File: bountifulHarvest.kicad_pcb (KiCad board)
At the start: 2 copper layers, 17 parts, among them U1 ATmega2560-16AU, U10 TMC2130-LA, U2 STM32F303CBTx, U3 TPS5431DDA, U4 AMS1117-3.3, U6 TMC2130-LA, U7 TMC2130-LA, U8 TMC2130-LA, U9 TMC2130-LA

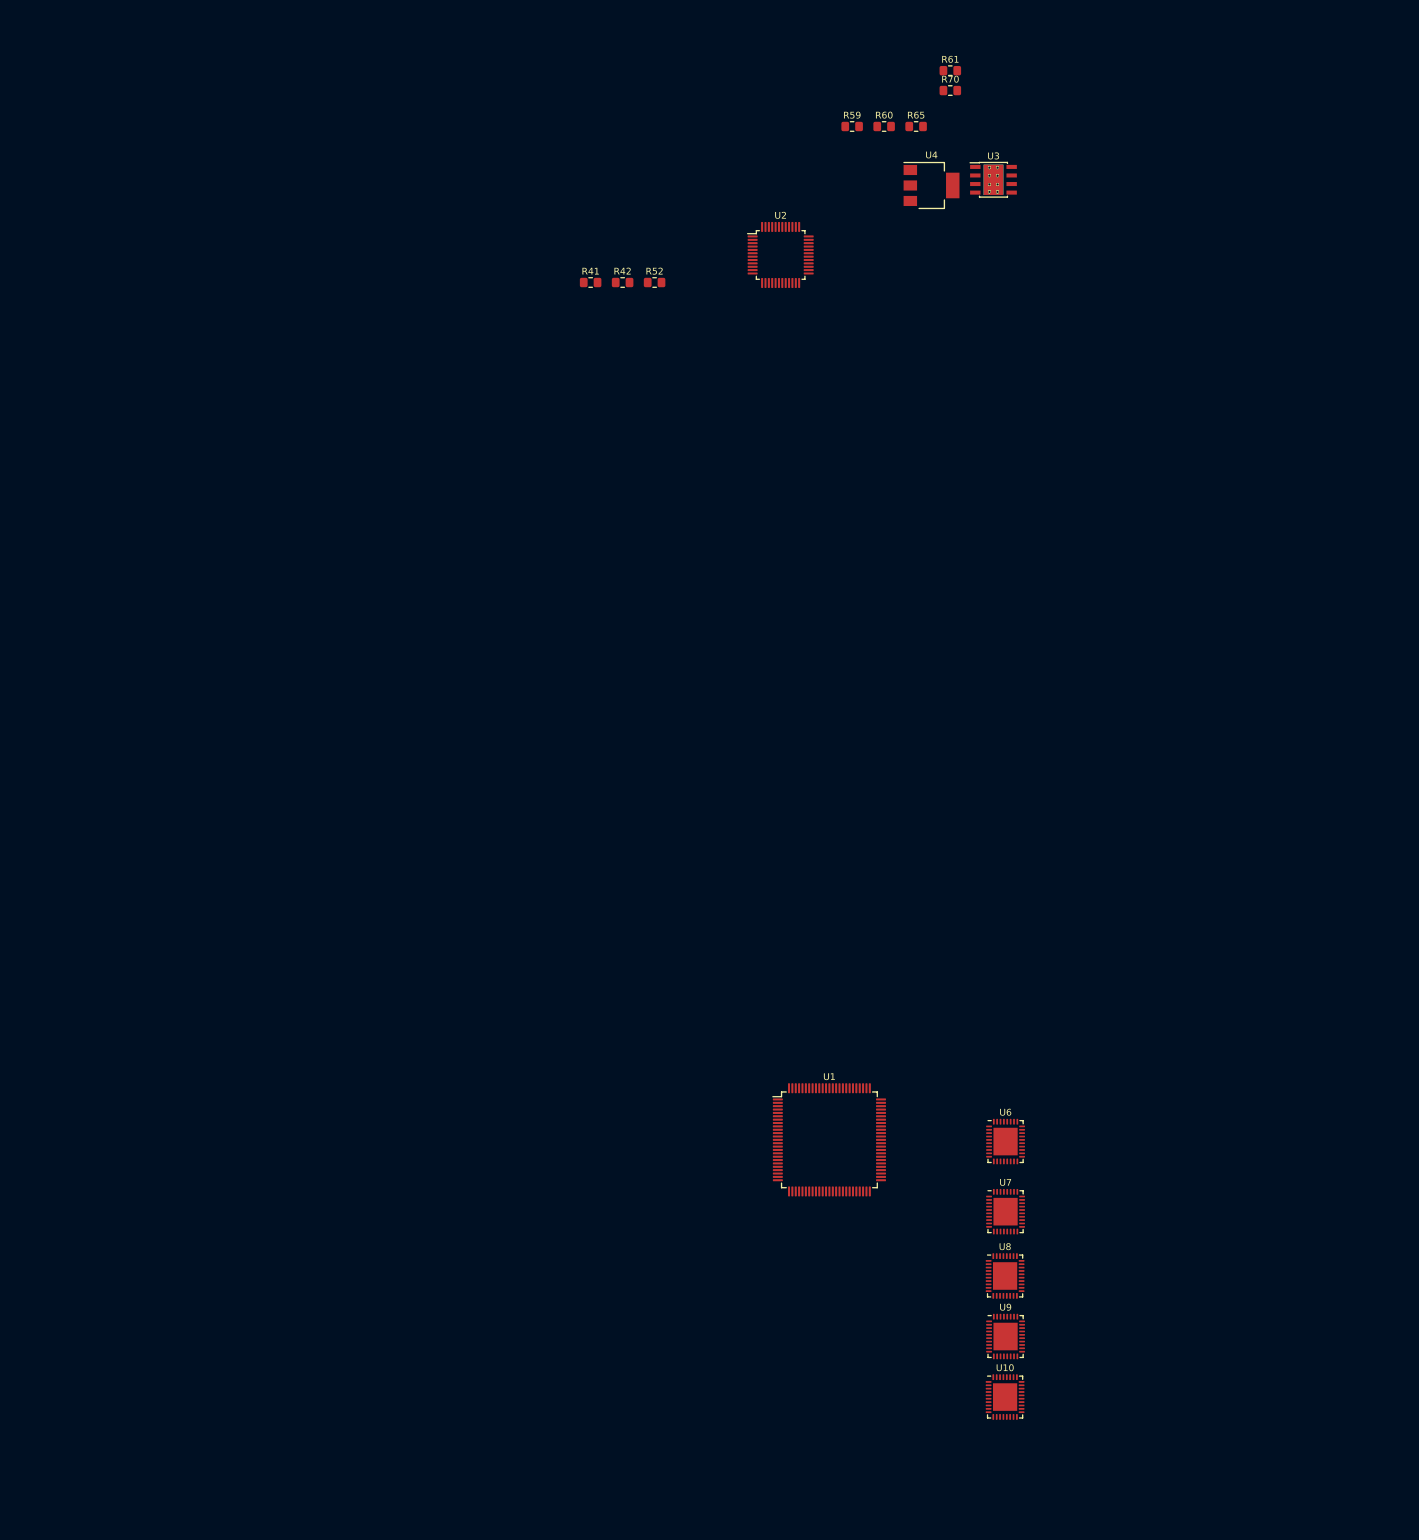
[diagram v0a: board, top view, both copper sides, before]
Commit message: Updated bus connections between drivers at ATMega
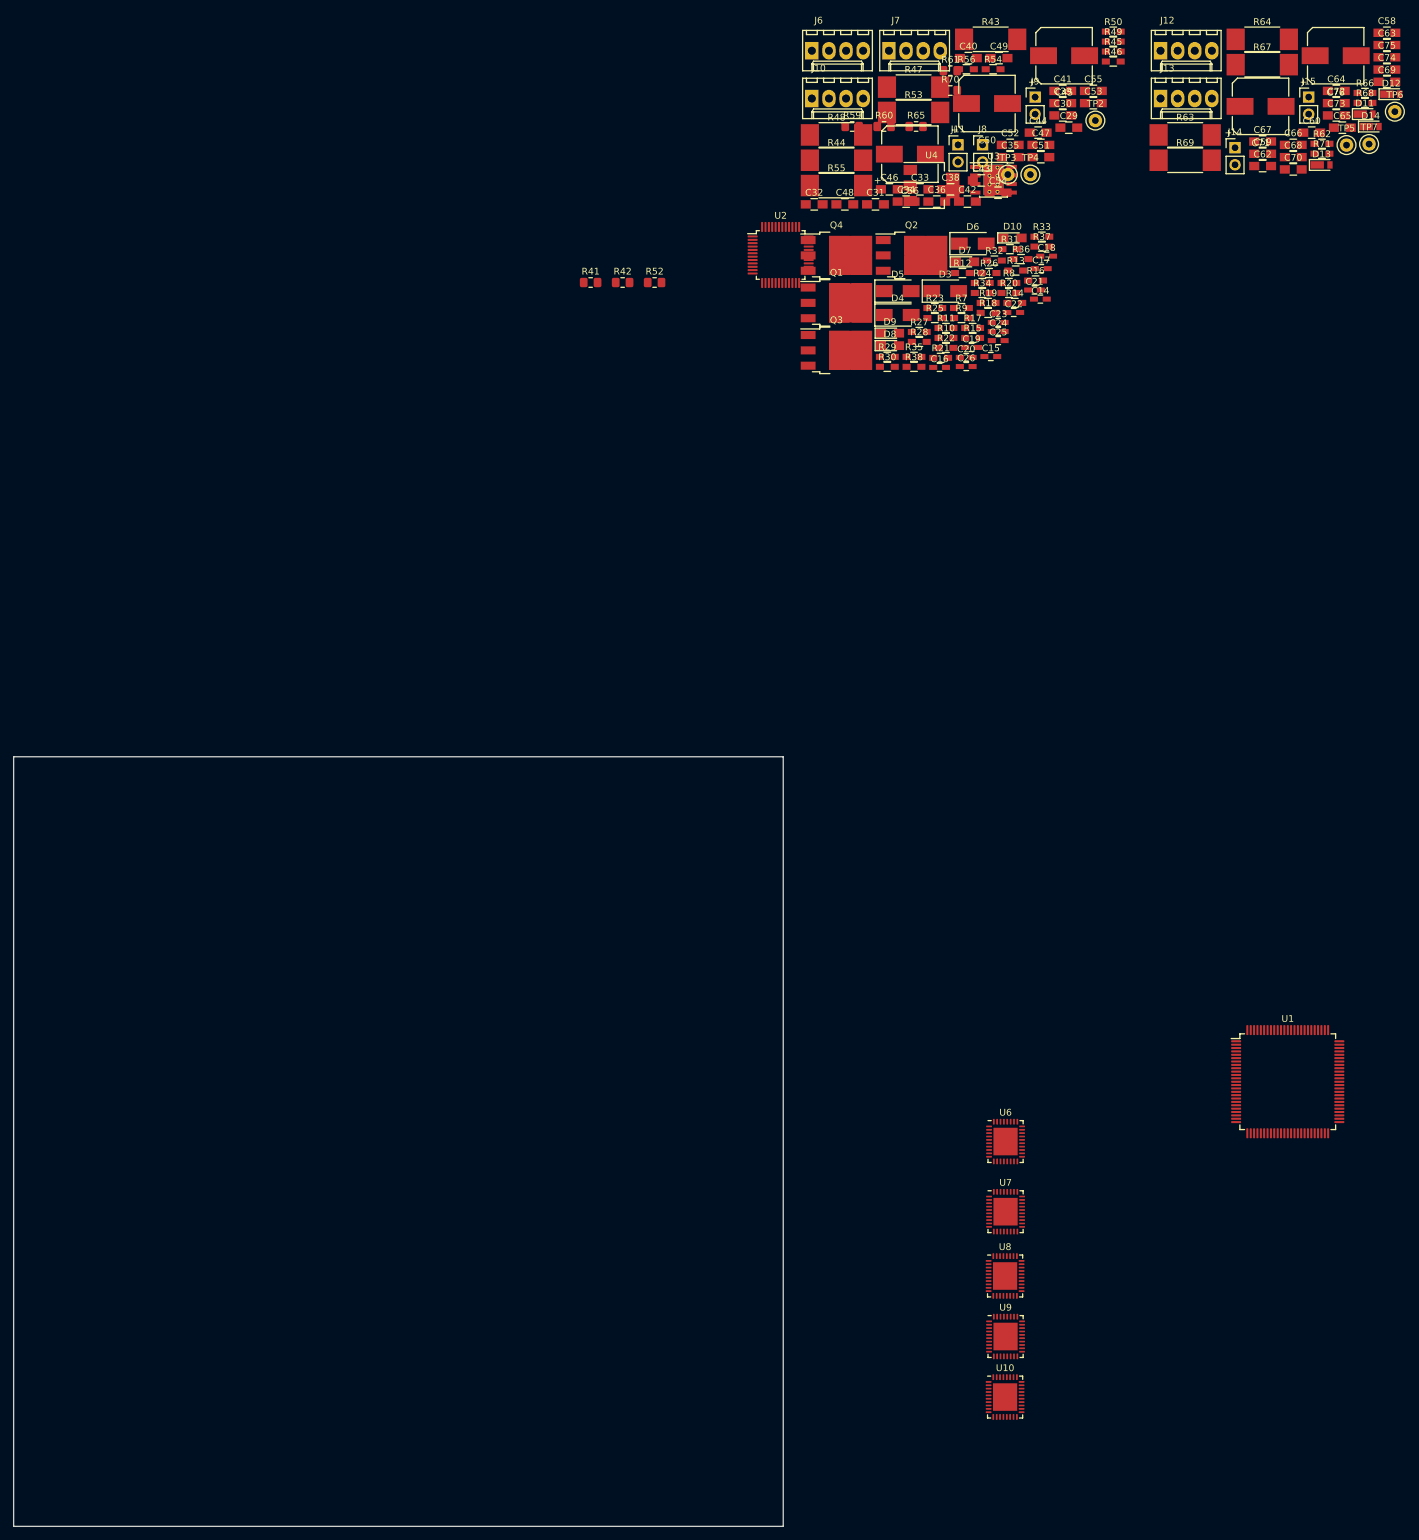
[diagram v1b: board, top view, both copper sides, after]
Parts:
- added C14: 1nF, Capacitors_SMD:C_0603_HandSoldering, F.Cu at (177.9, -42.6)
- added C15: 1nF, Capacitors_SMD:C_0603_HandSoldering, F.Cu at (170.5, -34.0)
- added C16: 1nF, Capacitors_SMD:C_0603_HandSoldering, F.Cu at (162.9, -32.4)
- added C17: 1nF, Capacitors_SMD:C_0603_HandSoldering, F.Cu at (178.0, -47.1)
- added C18: 100pF, Capacitors_SMD:C_0603_HandSoldering, F.Cu at (178.8, -48.9)
- added C19: 100pF, Capacitors_SMD:C_0603_HandSoldering, F.Cu at (167.7, -35.4)
- added C20: 100pF, Capacitors_SMD:C_0603_HandSoldering, F.Cu at (166.9, -33.9)
- added C21: 100pF, Capacitors_SMD:C_0603_HandSoldering, F.Cu at (177.0, -43.9)
- added C22: 100pF, Capacitors_SMD:C_0603_HandSoldering, F.Cu at (173.9, -40.6)
- added C23: 100pF, Capacitors_SMD:C_0603_HandSoldering, F.Cu at (171.6, -39.1)
- added C24: 100pF, Capacitors_SMD:C_0603_HandSoldering, F.Cu at (171.6, -37.8)
- added C25: 100pF, Capacitors_SMD:C_0603_HandSoldering, F.Cu at (171.6, -36.4)
- added C26: 1nF, Capacitors_SMD:C_0603_HandSoldering, F.Cu at (166.9, -32.6)
- added C29: 4.7uF, Capacitors_SMD:C_0805_HandSoldering, F.Cu at (182.1, -68.0)
- added C30: 4.7uF, Capacitors_SMD:C_0805_HandSoldering, F.Cu at (181.2, -69.9)
- added C31: 100nF, Capacitors_SMD:C_0805_HandSoldering, F.Cu at (153.4, -56.6)
- added C32: 100nF, Capacitors_SMD:C_0805_HandSoldering, F.Cu at (144.3, -56.6)
- added C33: 100nF, Capacitors_SMD:C_0805_HandSoldering, F.Cu at (160.0, -58.9)
- added C34: 100nF, Capacitors_SMD:C_0805_HandSoldering, F.Cu at (157.9, -57.1)
- added C35: 22nF, Capacitors_SMD:C_0805_HandSoldering, F.Cu at (173.4, -63.7)
- added C36: 22nF, Capacitors_SMD:C_0805_HandSoldering, F.Cu at (162.5, -57.1)
- added C38: 4.7uF, Capacitors_SMD:C_0805_HandSoldering, F.Cu at (164.6, -58.9)
- added C39: 100nF, Capacitors_SMD:C_0805_HandSoldering, F.Cu at (181.2, -71.7)
- added C40: 100nF, Capacitors_SMD:C_0805_HandSoldering, F.Cu at (167.2, -78.4)
- added C41: 100nF, Capacitors_SMD:C_0805_HandSoldering, F.Cu at (181.2, -73.5)
- added C42: 100nF, Capacitors_SMD:C_0805_HandSoldering, F.Cu at (167.0, -57.1)
- added C43: 100nF, Capacitors_SMD:C_0805_HandSoldering, F.Cu at (169.1, -60.2)
- added C44: 100nF, Capacitors_SMD:C_0805_HandSoldering, F.Cu at (177.6, -67.3)
- added C45: 100uF, Capacitors_SMD:CP_Elec_8x10, F.Cu at (181.4, -78.7)
- added C46: 100nF, Capacitors_SMD:C_0805_HandSoldering, F.Cu at (155.5, -58.9)
- added C47: 100nF, Capacitors_SMD:C_0805_HandSoldering, F.Cu at (178.0, -65.5)
- added C48: 100nF, Capacitors_SMD:C_0805_HandSoldering, F.Cu at (148.8, -56.6)
- added C49: 100nF, Capacitors_SMD:C_0805_HandSoldering, F.Cu at (171.7, -78.4)
- added C50: 100uF, Capacitors_SMD:CP_Elec_8x10, F.Cu at (170.0, -71.6)
- added C51: 22nF, Capacitors_SMD:C_0805_HandSoldering, F.Cu at (178.0, -63.7)
- added C52: 100nF, Capacitors_SMD:C_0805_HandSoldering, F.Cu at (173.4, -65.5)
- added C53: 100nF, Capacitors_SMD:C_0805_HandSoldering, F.Cu at (185.8, -71.7)
- added C54: 100nF, Capacitors_SMD:C_0805_HandSoldering, F.Cu at (171.6, -58.4)
- added C55: 100nF, Capacitors_SMD:C_0805_HandSoldering, F.Cu at (185.8, -73.5)
- added C56: 100uF, Capacitors_SMD:CP_Elec_8x10, F.Cu at (158.5, -64.1)
- added C58: 4.7uF, Capacitors_SMD:C_0805_HandSoldering, F.Cu at (229.3, -82.1)
- added C59: 100nF, Capacitors_SMD:C_0805_HandSoldering, F.Cu at (210.9, -64.2)
- added C60: 100nF, Capacitors_SMD:C_0805_HandSoldering, F.Cu at (218.2, -67.3)
- added C62: 4.7uF, Capacitors_SMD:C_0805_HandSoldering, F.Cu at (210.9, -62.3)
- added C63: 100nF, Capacitors_SMD:C_0805_HandSoldering, F.Cu at (229.3, -80.3)
- added C64: 100nF, Capacitors_SMD:C_0805_HandSoldering, F.Cu at (221.8, -73.5)
- added C65: 22nF, Capacitors_SMD:C_0805_HandSoldering, F.Cu at (222.7, -68.0)
- added C66: 22nF, Capacitors_SMD:C_0805_HandSoldering, F.Cu at (215.4, -65.5)
- added C67: 100nF, Capacitors_SMD:C_0805_HandSoldering, F.Cu at (210.9, -66.0)
- added C68: 100nF, Capacitors_SMD:C_0805_HandSoldering, F.Cu at (215.4, -63.7)
- added C69: 100nF, Capacitors_SMD:C_0805_HandSoldering, F.Cu at (229.3, -74.8)
- added C70: 100nF, Capacitors_SMD:C_0805_HandSoldering, F.Cu at (215.4, -61.8)
- added C71: 100uF, Capacitors_SMD:CP_Elec_8x10, F.Cu at (210.6, -71.2)
- added C72: 100nF, Capacitors_SMD:C_0805_HandSoldering, F.Cu at (221.8, -71.7)
- added C73: 100nF, Capacitors_SMD:C_0805_HandSoldering, F.Cu at (221.8, -69.9)
- added C74: 100nF, Capacitors_SMD:C_0805_HandSoldering, F.Cu at (229.3, -76.7)
- added C75: 100nF, Capacitors_SMD:C_0805_HandSoldering, F.Cu at (229.3, -78.5)
- added C76: 100uF, Capacitors_SMD:CP_Elec_8x10, F.Cu at (221.7, -78.7)
- added D10: LED, LEDs:LED_0805_HandSoldering, F.Cu at (173.7, -51.7)
- added D11: DNP, Diodes_SMD:D_TUMD2, F.Cu at (226.0, -70.0)
- added D12: DNP, Diodes_SMD:D_TUMD2, F.Cu at (230.0, -73.0)
- added D13: DNP, Diodes_SMD:D_TUMD2, F.Cu at (219.6, -62.5)
- added D14: DNP, Diodes_SMD:D_TUMD2, F.Cu at (226.9, -68.2)
- added D3: D_Zener, Diodes_SMD:D_SMA, F.Cu at (163.7, -43.8)
- added D4: D_Zener, Diodes_SMD:D_SMA, F.Cu at (156.7, -40.2)
- added D5: D_Zener, Diodes_SMD:D_SMA, F.Cu at (156.7, -43.8)
- added D6: D_Zener, Diodes_SMD:D_SMA, F.Cu at (167.8, -50.8)
- added D7: LED, LEDs:LED_0805_HandSoldering, F.Cu at (166.7, -48.1)
- added D8: LED, LEDs:LED_0805_HandSoldering, F.Cu at (155.5, -35.7)
- added D9: LED, LEDs:LED_0805_HandSoldering, F.Cu at (155.5, -37.5)
- added J10: CHECK FOOTPRINT, Connectors_Molex:Molex_KK-6410-04_04x2.54mm_Straight, F.Cu at (143.9, -72.4)
- added J11: Conn_01x02_Male, Pin_Headers:Pin_Header_Straight_1x02_Pitch2.54mm, F.Cu at (165.7, -65.5)
- added J12: CHECK FOOTPRINT, Connectors_Molex:Molex_KK-6410-04_04x2.54mm_Straight, F.Cu at (195.7, -79.5)
- added J13: CHECK FOOTPRINT, Connectors_Molex:Molex_KK-6410-04_04x2.54mm_Straight, F.Cu at (195.7, -72.4)
- added J14: Conn_01x02_Male, Pin_Headers:Pin_Header_Straight_1x02_Pitch2.54mm, F.Cu at (206.8, -65.1)
- added J15: Conn_01x02_Male, Pin_Headers:Pin_Header_Straight_1x02_Pitch2.54mm, F.Cu at (217.7, -72.6)
- added J6: CHECK FOOTPRINT, Connectors_Molex:Molex_KK-6410-04_04x2.54mm_Straight, F.Cu at (143.9, -79.5)
- added J7: CHECK FOOTPRINT, Connectors_Molex:Molex_KK-6410-04_04x2.54mm_Straight, F.Cu at (155.4, -79.5)
- added J8: Conn_01x02_Male, Pin_Headers:Pin_Header_Straight_1x02_Pitch2.54mm, F.Cu at (169.3, -65.5)
- added J9: Conn_01x02_Male, Pin_Headers:Pin_Header_Straight_1x02_Pitch2.54mm, F.Cu at (177.1, -72.6)
- added Q1: Q_NMOS_GDSD, TO_SOT_Packages_SMD:TO-252-3_TabPin2, F.Cu at (147.6, -42.0)
- added Q2: Q_NMOS_GDSD, TO_SOT_Packages_SMD:TO-252-3_TabPin2, F.Cu at (158.7, -49.1)
- added Q3: Q_NMOS_GDSD, TO_SOT_Packages_SMD:TO-252-3_TabPin2, F.Cu at (147.6, -35.0)
- added Q4: Q_NMOS_GDSD, TO_SOT_Packages_SMD:TO-252-3_TabPin2, F.Cu at (147.6, -49.1)
- added R10: 10k, Resistors_SMD:R_0603_HandSoldering, F.Cu at (163.9, -36.8)
- added R11: 10, Resistors_SMD:R_0603_HandSoldering, F.Cu at (163.9, -38.3)
- added R12: 10, Resistors_SMD:R_0603_HandSoldering, F.Cu at (166.3, -46.4)
- added R13: 10k, Resistors_SMD:R_0603_HandSoldering, F.Cu at (174.2, -46.8)
- added R14: 10, Resistors_SMD:R_0603_HandSoldering, F.Cu at (174.1, -42.0)
- added R15: 10k, Resistors_SMD:R_0603_HandSoldering, F.Cu at (167.8, -36.8)
- added R16: 10, Resistors_SMD:R_0603_HandSoldering, F.Cu at (177.2, -45.3)
- added R17: 10k, Resistors_SMD:R_0603_HandSoldering, F.Cu at (167.8, -38.3)
- added R18: 10k, Resistors_SMD:R_0603_HandSoldering, F.Cu at (170.1, -40.5)
- added R19: .02, Resistors_SMD:R_0603_HandSoldering, F.Cu at (170.1, -42.0)
- added R20: .02, Resistors_SMD:R_0603_HandSoldering, F.Cu at (173.2, -43.5)
- added R21: .02, Resistors_SMD:R_0603_HandSoldering, F.Cu at (163.1, -33.8)
- added R22: .02, Resistors_SMD:R_0603_HandSoldering, F.Cu at (163.9, -35.3)
- added R23: 1k, Resistors_SMD:R_0603_HandSoldering, F.Cu at (162.2, -41.2)
- added R24: 1k, Resistors_SMD:R_0603_HandSoldering, F.Cu at (169.3, -45.0)
- added R25: 1k, Resistors_SMD:R_0603_HandSoldering, F.Cu at (162.2, -39.8)
- added R26: 1k, Resistors_SMD:R_0603_HandSoldering, F.Cu at (170.3, -46.4)
- added R27: 1k, Resistors_SMD:R_0603_HandSoldering, F.Cu at (159.9, -37.7)
- added R28: 1k, Resistors_SMD:R_0603_HandSoldering, F.Cu at (159.9, -36.2)
- added R29: 1k, Resistors_SMD:R_0603_HandSoldering, F.Cu at (155.2, -34.0)
- added R30: 1k, Resistors_SMD:R_0603_HandSoldering, F.Cu at (155.2, -32.5)
- added R31: 1k, Resistors_SMD:R_0603_HandSoldering, F.Cu at (173.4, -50.0)
- added R32: 33k, Resistors_SMD:R_0603_HandSoldering, F.Cu at (171.1, -48.3)
- added R33: 33k, Resistors_SMD:R_0603_HandSoldering, F.Cu at (178.1, -51.8)
- added R34: 33k, Resistors_SMD:R_0603_HandSoldering, F.Cu at (169.3, -43.5)
- added R35: 1k, Resistors_SMD:R_0603_HandSoldering, F.Cu at (159.1, -34.0)
- added R36: 1k, Resistors_SMD:R_0603_HandSoldering, F.Cu at (175.0, -48.5)
- added R37: 1k, Resistors_SMD:R_0603_HandSoldering, F.Cu at (178.1, -50.4)
- added R38: 33k, Resistors_SMD:R_0603_HandSoldering, F.Cu at (159.1, -32.5)
- added R43: 120m, Resistors_SMD:R_2512_HandSoldering, F.Cu at (170.5, -81.2)
- added R44: 120m, Resistors_SMD:R_2512_HandSoldering, F.Cu at (147.6, -63.2)
- added R45: 10k, Resistors_SMD:R_0603_HandSoldering, F.Cu at (188.7, -79.3)
- added R46: 10k, Resistors_SMD:R_0603_HandSoldering, F.Cu at (188.7, -77.9)
- added R47: 120m, Resistors_SMD:R_2512_HandSoldering, F.Cu at (159.1, -74.1)
- added R48: 120m, Resistors_SMD:R_2512_HandSoldering, F.Cu at (147.6, -67.0)
- added R49: 10k, Resistors_SMD:R_0603_HandSoldering, F.Cu at (188.7, -80.8)
- added R50: 10k, Resistors_SMD:R_0603_HandSoldering, F.Cu at (188.7, -82.3)
- added R53: 120m, Resistors_SMD:R_2512_HandSoldering, F.Cu at (159.1, -70.3)
- added R54: 10k, Resistors_SMD:R_0603_HandSoldering, F.Cu at (170.9, -76.7)
- added R55: 120m, Resistors_SMD:R_2512_HandSoldering, F.Cu at (147.6, -59.4)
- added R56: 10k, Resistors_SMD:R_0603_HandSoldering, F.Cu at (166.9, -76.7)
- added R62: 10k, Resistors_SMD:R_0603_HandSoldering, F.Cu at (219.7, -65.6)
- added R63: 120m, Resistors_SMD:R_2512_HandSoldering, F.Cu at (199.4, -67.0)
- added R64: 120m, Resistors_SMD:R_2512_HandSoldering, F.Cu at (210.8, -81.2)
- added R66: 10k, Resistors_SMD:R_0603_HandSoldering, F.Cu at (226.1, -73.2)
- added R67: 120m, Resistors_SMD:R_2512_HandSoldering, F.Cu at (210.8, -77.4)
- added R68: 10k, Resistors_SMD:R_0603_HandSoldering, F.Cu at (226.1, -71.7)
- added R69: 120m, Resistors_SMD:R_2512_HandSoldering, F.Cu at (199.4, -63.2)
- added R7: 10k, Resistors_SMD:R_0603_HandSoldering, F.Cu at (166.2, -41.2)
- added R71: 10k, Resistors_SMD:R_0603_HandSoldering, F.Cu at (219.7, -64.2)
- added R8: 10k, Resistors_SMD:R_0603_HandSoldering, F.Cu at (173.2, -45.0)
- added R9: 10k, Resistors_SMD:R_0603_HandSoldering, F.Cu at (166.2, -39.8)
- added TP2: TestPoint, Measurement_Points:Test_Point_Keystone_5000-5004_Miniature, F.Cu at (186.1, -69.1)
- added TP3: TestPoint, Measurement_Points:Test_Point_Keystone_5000-5004_Miniature, F.Cu at (173.1, -61.1)
- added TP4: TestPoint, Measurement_Points:Test_Point_Keystone_5000-5004_Miniature, F.Cu at (176.4, -61.1)
- added TP5: TestPoint, Measurement_Points:Test_Point_Keystone_5000-5004_Miniature, F.Cu at (223.4, -65.4)
- added TP6: TestPoint, Measurement_Points:Test_Point_Keystone_5000-5004_Miniature, F.Cu at (230.5, -70.4)
- added TP7: TestPoint, Measurement_Points:Test_Point_Keystone_5000-5004_Miniature, F.Cu at (226.7, -65.6)
- moved U1 68.6 mm to (214.6, 73.7)
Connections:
- U1 pad 1: Net-(U1-Pad1) -> (no net)
- U1 pad 100: Net-(U1-Pad100) -> (no net)
- U1 pad 12: Net-(U1-Pad12) -> (no net)
- U1 pad 13: Net-(U1-Pad13) -> (no net)
- U1 pad 14: Net-(U1-Pad14) -> (no net)
- U1 pad 15: Net-(U1-Pad15) -> (no net)
- U1 pad 16: Net-(U1-Pad16) -> (no net)
- U1 pad 17: Net-(U1-Pad17) -> (no net)
- U1 pad 18: Net-(U1-Pad18) -> (no net)
- U1 pad 19: Net-(R2-Pad2) -> (no net)
- U1 pad 2: Net-(U1-Pad2) -> (no net)
- U1 pad 24: Net-(U1-Pad24) -> (no net)
- U1 pad 25: Net-(U1-Pad25) -> (no net)
- U1 pad 26: Net-(U1-Pad26) -> (no net)
- U1 pad 27: Net-(U1-Pad27) -> (no net)
- U1 pad 28: Net-(U1-Pad28) -> (no net)
- U1 pad 29: Net-(U1-Pad29) -> (no net)
- U1 pad 3: Net-(U1-Pad3) -> (no net)
- U1 pad 30: Net-(U1-Pad30) -> (no net)
- U1 pad 33: Net-(U1-Pad33) -> (no net)
- U1 pad 34: Net-(U1-Pad34) -> (no net)
- U1 pad 35: Net-(U1-Pad35) -> (no net)
- U1 pad 36: Net-(U1-Pad36) -> (no net)
- U1 pad 37: Net-(U1-Pad37) -> (no net)
- U1 pad 38: Net-(U1-Pad38) -> (no net)
- U1 pad 39: Net-(U1-Pad39) -> (no net)
- U1 pad 4: Net-(U1-Pad4) -> (no net)
- U1 pad 40: Net-(U1-Pad40) -> (no net)
- U1 pad 41: Net-(U1-Pad41) -> (no net)
- U1 pad 42: Net-(U1-Pad42) -> (no net)
- U1 pad 43: Net-(U1-Pad43) -> (no net)
- U1 pad 44: Net-(U1-Pad44) -> (no net)
- U1 pad 45: Net-(U1-Pad45) -> (no net)
- U1 pad 46: Net-(U1-Pad46) -> (no net)
- U1 pad 47: Net-(U1-Pad47) -> (no net)
- U1 pad 48: Net-(U1-Pad48) -> (no net)
- U1 pad 49: Net-(U1-Pad49) -> (no net)
- U1 pad 5: Net-(U1-Pad5) -> (no net)
- U1 pad 50: Net-(U1-Pad50) -> (no net)
- U1 pad 51: Net-(U1-Pad51) -> (no net)
- U1 pad 52: Net-(U1-Pad52) -> (no net)
- U1 pad 53: Net-(U1-Pad53) -> (no net)
- U1 pad 54: Net-(U1-Pad54) -> (no net)
- U1 pad 55: Net-(U1-Pad55) -> (no net)
- U1 pad 56: Net-(U1-Pad56) -> (no net)
- U1 pad 57: Net-(U1-Pad57) -> (no net)
- U1 pad 58: Net-(U1-Pad58) -> (no net)
- U1 pad 59: Net-(U1-Pad59) -> (no net)
- U1 pad 6: Net-(U1-Pad6) -> (no net)
- U1 pad 60: Net-(U1-Pad60) -> (no net)
- U1 pad 63: Net-(U1-Pad63) -> (no net)
- U1 pad 64: Net-(U1-Pad64) -> (no net)
- U1 pad 65: Net-(U1-Pad65) -> (no net)
- U1 pad 66: Net-(U1-Pad66) -> (no net)
- U1 pad 67: Net-(U1-Pad67) -> (no net)
- U1 pad 68: Net-(U1-Pad68) -> (no net)
- U1 pad 69: Net-(U1-Pad69) -> (no net)
- U1 pad 7: Net-(U1-Pad7) -> (no net)
- U1 pad 70: Net-(U1-Pad70) -> (no net)
- U1 pad 71: Net-(U1-Pad71) -> (no net)
- U1 pad 72: Net-(U1-Pad72) -> (no net)
- U1 pad 73: Net-(U1-Pad73) -> (no net)
- U1 pad 74: Net-(U1-Pad74) -> (no net)
- U1 pad 75: Net-(U1-Pad75) -> (no net)
- U1 pad 76: Net-(U1-Pad76) -> (no net)
- U1 pad 77: Net-(U1-Pad77) -> (no net)
- U1 pad 78: /Main Processor/~SS_cop -> (no net)
- U1 pad 79: Net-(U1-Pad79) -> (no net)
- U1 pad 8: Net-(U1-Pad8) -> (no net)
- U1 pad 82: Net-(U1-Pad82) -> (no net)
- U1 pad 83: Net-(U1-Pad83) -> (no net)
- U1 pad 84: Net-(U1-Pad84) -> (no net)
- U1 pad 85: Net-(U1-Pad85) -> (no net)
- U1 pad 86: Net-(U1-Pad86) -> (no net)
- U1 pad 87: Net-(U1-Pad87) -> (no net)
- U1 pad 88: Net-(U1-Pad88) -> (no net)
- U1 pad 89: Net-(U1-Pad89) -> (no net)
- U1 pad 9: Net-(U1-Pad9) -> (no net)
- U1 pad 90: Net-(U1-Pad90) -> (no net)
- U1 pad 91: Net-(U1-Pad91) -> (no net)
- U1 pad 92: Net-(U1-Pad92) -> (no net)
- U1 pad 93: Net-(U1-Pad93) -> (no net)
- U1 pad 94: Net-(U1-Pad94) -> (no net)
- U1 pad 95: Net-(U1-Pad95) -> (no net)
- U1 pad 96: Net-(U1-Pad96) -> (no net)
- U1 pad 97: Net-(U1-Pad97) -> (no net)
- U1 pad 98: Net-(U1-Pad98) -> (no net)
- U10 pad 10: Net-(U10-Pad10) -> (no net)
- U10 pad 17: Net-(U10-Pad17) -> (no net)
- U10 pad 19: Net-(U10-Pad19) -> (no net)
- U10 pad 2: /Spare/~CS~_SPI_X2 -> (no net)
- U10 pad 22: /Spare/EN_X2 -> (no net)
- U10 pad 30: Net-(U10-Pad30) -> (no net)
- U10 pad 6: /Spare/STEP_X2 -> (no net)
- U10 pad 7: /Spare/DIR_X2 -> (no net)
- U10 pad 9: Net-(U10-Pad9) -> (no net)
- U2 pad 1: Net-(U2-Pad1) -> (no net)
- U2 pad 10: Net-(U2-Pad10) -> (no net)
- U2 pad 11: Net-(U2-Pad11) -> (no net)
- U2 pad 12: Net-(U2-Pad12) -> (no net)
- U2 pad 13: Net-(U2-Pad13) -> (no net)
- U2 pad 14: Net-(U2-Pad14) -> (no net)
- U2 pad 15: Net-(U2-Pad15) -> (no net)
- U2 pad 16: Net-(U2-Pad16) -> (no net)
- U2 pad 17: Net-(U2-Pad17) -> (no net)
- U2 pad 18: Net-(U2-Pad18) -> (no net)
- U2 pad 19: Net-(U2-Pad19) -> (no net)
- U2 pad 2: Net-(U2-Pad2) -> (no net)
- U2 pad 20: Net-(U2-Pad20) -> (no net)
- U2 pad 21: Net-(U2-Pad21) -> (no net)
- U2 pad 22: Net-(U2-Pad22) -> (no net)
- U2 pad 23: Net-(U2-Pad23) -> (no net)
- U2 pad 24: Net-(U2-Pad24) -> (no net)
- U2 pad 25: Net-(U2-Pad25) -> (no net)
- U2 pad 26: Net-(U2-Pad26) -> (no net)
- U2 pad 27: Net-(U2-Pad27) -> (no net)
- U2 pad 28: Net-(U2-Pad28) -> (no net)
- U2 pad 29: Net-(U2-Pad29) -> (no net)
- U2 pad 3: Net-(U2-Pad3) -> (no net)
- U2 pad 30: Net-(U2-Pad30) -> (no net)
- U2 pad 31: Net-(U2-Pad31) -> (no net)
- U2 pad 32: Net-(U2-Pad32) -> (no net)
- U2 pad 33: Net-(U2-Pad33) -> (no net)
- U2 pad 34: Net-(U2-Pad34) -> (no net)
- U2 pad 35: Net-(U2-Pad35) -> (no net)
- U2 pad 36: Net-(U2-Pad36) -> (no net)
- U2 pad 37: Net-(U2-Pad37) -> (no net)
- U2 pad 38: Net-(U2-Pad38) -> (no net)
- U2 pad 39: Net-(U2-Pad39) -> (no net)
- U2 pad 4: Net-(U2-Pad4) -> (no net)
- U2 pad 40: Net-(U2-Pad40) -> (no net)
- U2 pad 41: Net-(U2-Pad41) -> (no net)
- U2 pad 42: Net-(U2-Pad42) -> (no net)
- U2 pad 43: Net-(U2-Pad43) -> (no net)
- U2 pad 44: Net-(U2-Pad44) -> (no net)
- U2 pad 45: Net-(U2-Pad45) -> (no net)
- U2 pad 46: Net-(U2-Pad46) -> (no net)
- U2 pad 47: Net-(U2-Pad47) -> (no net)
- U2 pad 48: Net-(U2-Pad48) -> (no net)
- U2 pad 5: Net-(U2-Pad5) -> (no net)
- U2 pad 6: Net-(U2-Pad6) -> (no net)
- U2 pad 7: Net-(U2-Pad7) -> (no net)
- U2 pad 8: Net-(U2-Pad8) -> (no net)
- U2 pad 9: Net-(U2-Pad9) -> (no net)
- U3 pad 1: Net-(C1-Pad2) -> (no net)
- U3 pad 2: Net-(U3-Pad2) -> (no net)
- U3 pad 3: Net-(U3-Pad3) -> (no net)
- U3 pad 4: Net-(R4-Pad2) -> (no net)
- U3 pad 5: Net-(R3-Pad2) -> (no net)
- U3 pad 7: Net-(C2-Pad1) -> (no net)
- U3 pad 8: Net-(C1-Pad1) -> (no net)
- U6 pad 10: Net-(U6-Pad10) -> (no net)
- U6 pad 17: Net-(U6-Pad17) -> (no net)
- U6 pad 19: Net-(U6-Pad19) -> (no net)
- U6 pad 2: /Drivers/~CS~_SPI_Y -> (no net)
- U6 pad 22: /Drivers/EN_Y -> (no net)
- U6 pad 30: Net-(U6-Pad30) -> (no net)
- U6 pad 6: /Drivers/STEP_Y -> (no net)
- U6 pad 7: /Drivers/DIR_Y -> (no net)
- U6 pad 9: Net-(U6-Pad9) -> (no net)
- U7 pad 10: Net-(U7-Pad10) -> (no net)
- U7 pad 17: Net-(U7-Pad17) -> (no net)
- U7 pad 19: Net-(U7-Pad19) -> (no net)
- U7 pad 2: /Drivers/~CS~_SPI_X -> (no net)
- U7 pad 22: /Drivers/EN_X -> (no net)
- U7 pad 30: Net-(U7-Pad30) -> (no net)
- U7 pad 6: /Drivers/STEP_X -> (no net)
- U7 pad 7: /Drivers/DIR_X -> (no net)
- U7 pad 9: Net-(U7-Pad9) -> (no net)
- U8 pad 10: Net-(U8-Pad10) -> (no net)
- U8 pad 17: Net-(U8-Pad17) -> (no net)
- U8 pad 19: Net-(U8-Pad19) -> (no net)
- U8 pad 2: /Drivers/~CS~_SPI_Z -> (no net)
- U8 pad 22: /Drivers/EN_Z -> (no net)
- U8 pad 30: Net-(U8-Pad30) -> (no net)
- U8 pad 6: /Drivers/STEP_Z -> (no net)
- U8 pad 7: /Drivers/DIR_Z -> (no net)
- U8 pad 9: Net-(U8-Pad9) -> (no net)
- U9 pad 10: Net-(U9-Pad10) -> (no net)
- U9 pad 17: Net-(U9-Pad17) -> (no net)
- U9 pad 19: Net-(U9-Pad19) -> (no net)
- U9 pad 22: /Spare/EN_SPARE -> (no net)
- U9 pad 30: Net-(U9-Pad30) -> (no net)
- U9 pad 6: /Spare/STEP_SPARE -> (no net)
- U9 pad 7: /Spare/DIR_SPARE -> (no net)
- U9 pad 9: Net-(U9-Pad9) -> (no net)
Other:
- board outline added: 114.3 x 114.3 mm

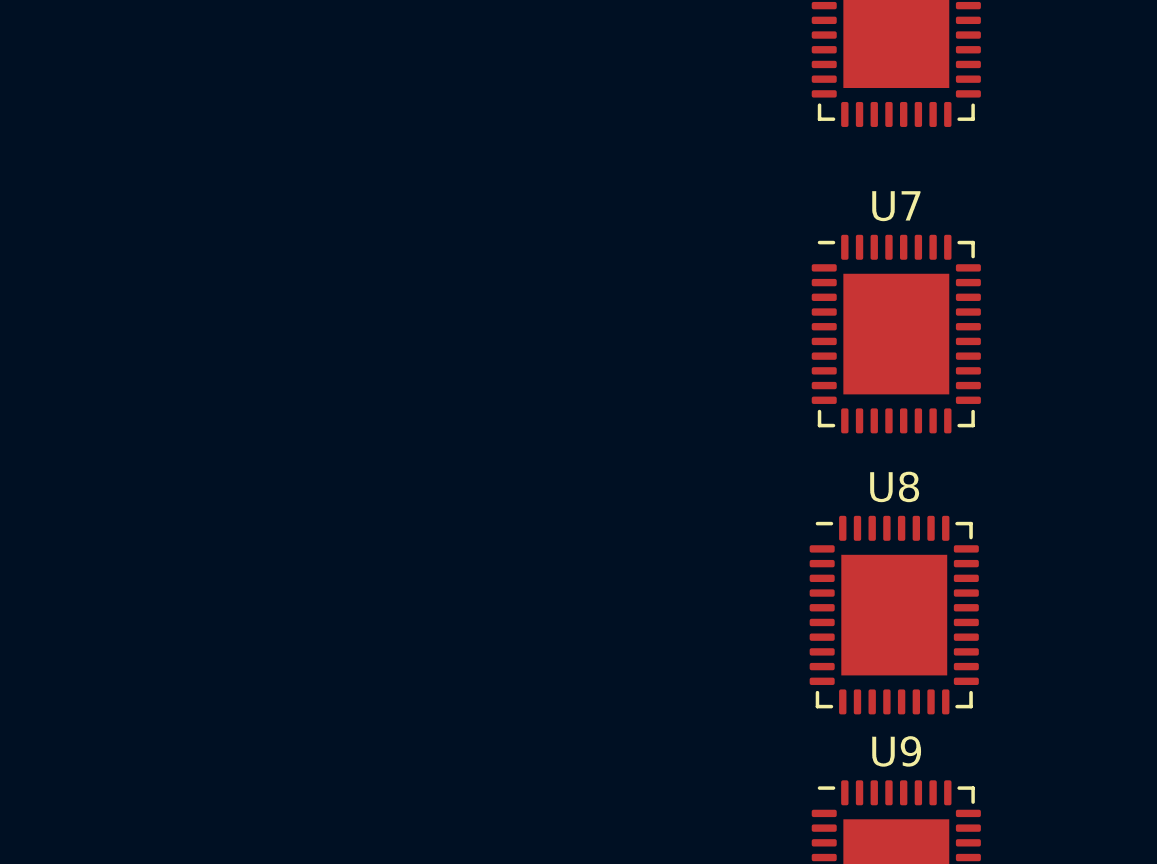
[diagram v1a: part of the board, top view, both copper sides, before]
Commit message: Fixed X,Y,Z driver bus connection. set up spare and X2
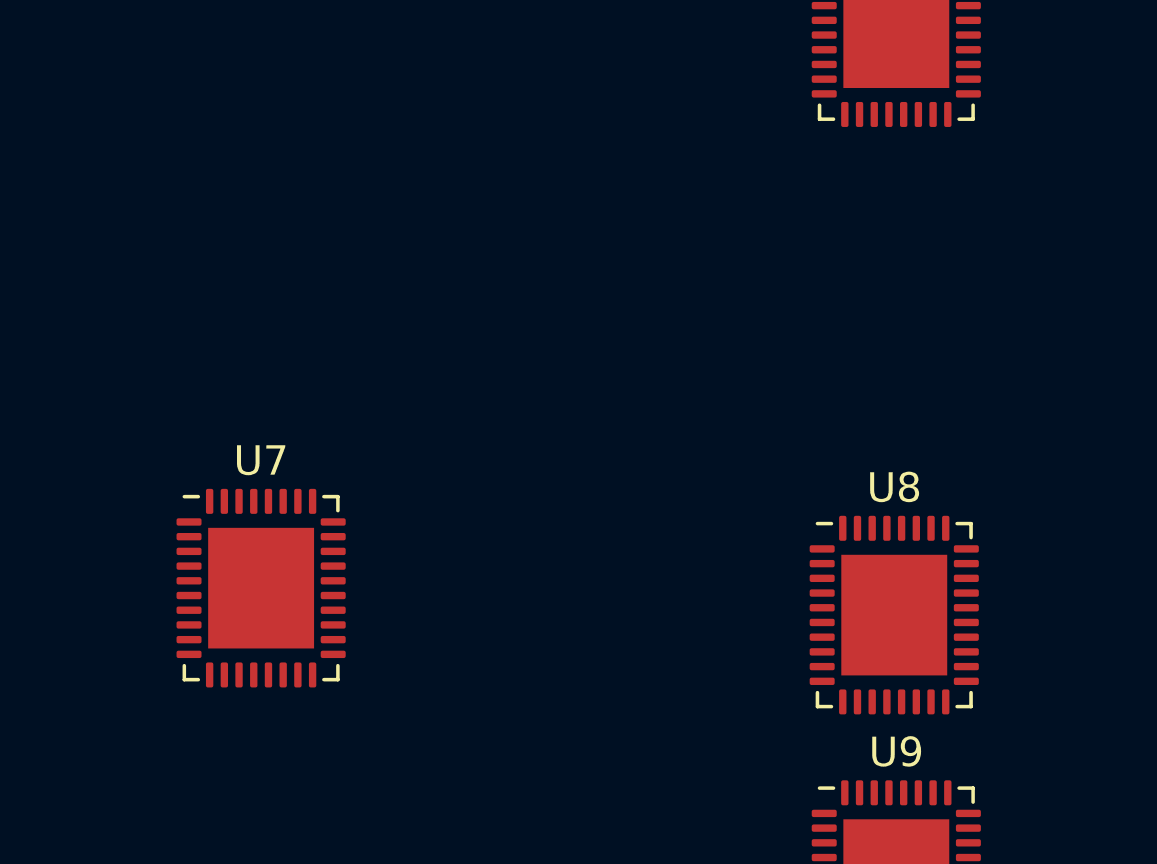
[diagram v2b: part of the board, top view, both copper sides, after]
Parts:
- moved U7 23.3 mm to (151.1, 101.6)
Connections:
- R41 pad 2: /Drivers/Y_DIAG -> /Drivers/Y_4
- R42 pad 2: /Drivers/X_DIAG -> /Drivers/X_4
- R52 pad 2: /Drivers/DIAG_Z -> /Drivers/Z_4
- TP2 pad 1: /Drivers/Y_DIAG -> /Drivers/Y_4
- TP3 pad 1: /Drivers/X_DIAG -> /Drivers/X_4
- TP4 pad 1: /Drivers/DIAG_Z -> /Drivers/Z_4
- U1 pad 12: (no net) -> /Drivers/Z_0
- U1 pad 13: (no net) -> /Drivers/Z_1
- U1 pad 14: (no net) -> /Drivers/Z_2
- U1 pad 15: (no net) -> /Drivers/Z_3
- U1 pad 16: (no net) -> /Drivers/Z_4
- U1 pad 2: (no net) -> /Drivers/Y_0
- U1 pad 20: /Main Processor/~CS~_SPI_SPARE -> (no net)
- U1 pad 21: /Drivers/SCK_SPI -> (no net)
- U1 pad 22: /Drivers/SDI_SPI -> (no net)
- U1 pad 23: /Drivers/SDO_SPI -> (no net)
- U1 pad 3: (no net) -> /Drivers/STEP_Y
- U1 pad 4: (no net) -> /Drivers/DIR_Y
- U1 pad 46: (no net) -> /Drivers/X_0
- U1 pad 47: (no net) -> /Drivers/STEP_X
- U1 pad 48: (no net) -> /Drivers/DIR_Y
- U1 pad 49: (no net) -> /Drivers/EN_X
- U1 pad 5: (no net) -> /Drivers/EN_Y
- U1 pad 50: (no net) -> /Drivers/X_4
- U1 pad 6: (no net) -> /Drivers/Y_4
- U6 pad 2: (no net) -> /Drivers/Y_0
- U6 pad 20: /Drivers/Y_DIAG -> /Drivers/Y_4
- U6 pad 21: /Drivers/Y_DIAG -> /Drivers/Y_4
- U6 pad 22: (no net) -> /Drivers/EN_Y
- U6 pad 6: (no net) -> /Drivers/STEP_Y
- U6 pad 7: (no net) -> /Drivers/DIR_Y
- U7 pad 2: (no net) -> /Drivers/X_0
- U7 pad 20: /Drivers/X_DIAG -> /Drivers/X_4
- U7 pad 21: /Drivers/X_DIAG -> /Drivers/X_4
- U7 pad 22: (no net) -> /Drivers/EN_X
- U7 pad 6: (no net) -> /Drivers/STEP_X
- U7 pad 7: (no net) -> /Drivers/DIR_Y
- U8 pad 2: (no net) -> /Drivers/Z_0
- U8 pad 20: /Drivers/DIAG_Z -> /Drivers/Z_4
- U8 pad 21: /Drivers/DIAG_Z -> /Drivers/Z_4
- U8 pad 22: (no net) -> /Drivers/Z_3
- U8 pad 6: (no net) -> /Drivers/Z_1
- U8 pad 7: (no net) -> /Drivers/Z_2
- U9 pad 2: /Main Processor/~CS~_SPI_SPARE -> (no net)
